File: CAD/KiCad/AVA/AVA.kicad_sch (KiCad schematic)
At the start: 44 parts, among them J1 Conn_01x03_Pin, J10 Conn_01x04_Pin, J2 Conn_01x03_Pin, J3 Conn_01x03_Pin, J4 Conn_01x03_Pin, J5 Conn_01x02_Pin, J6 Conn_01x02_Pin, J7 Conn_01x02_Pin, J8 Conn_01x03_Pin, J9 Conn_01x03_Pin, U1 WEMOS_C3_mini

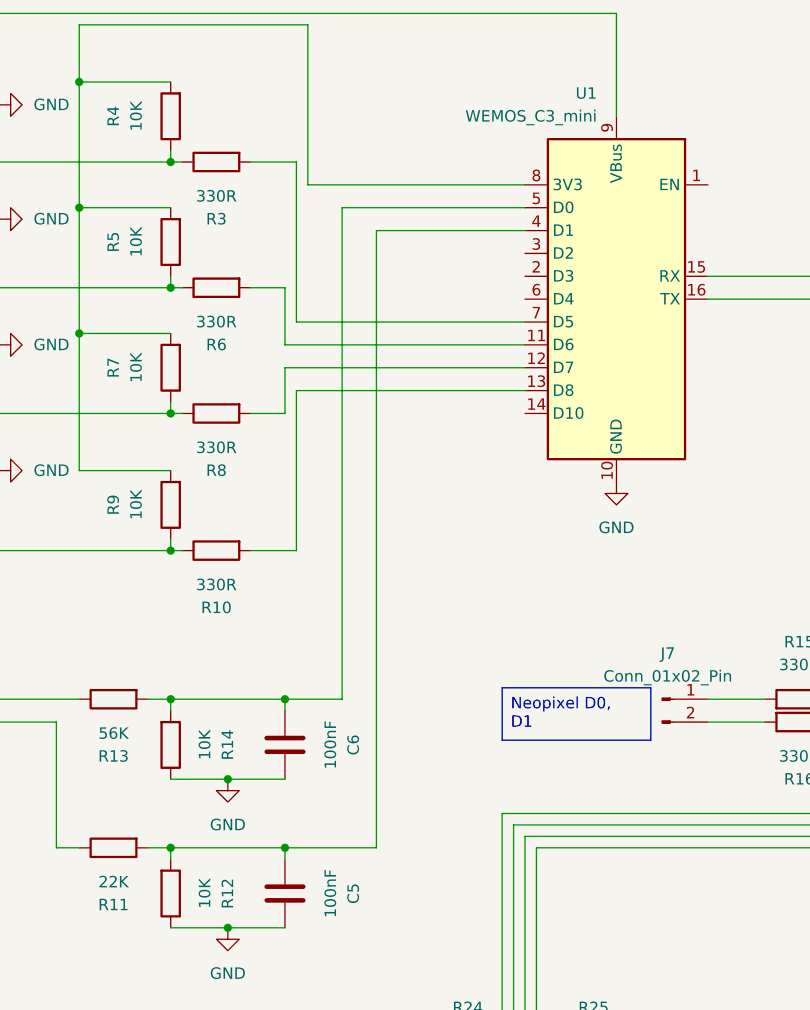
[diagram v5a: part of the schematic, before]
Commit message: Added PCB constraints from other projects which used photomedia etching of layout. Works good enough, 0.35mm track width min and 0.65mm clearance most important. Or else high chance of copper bridges
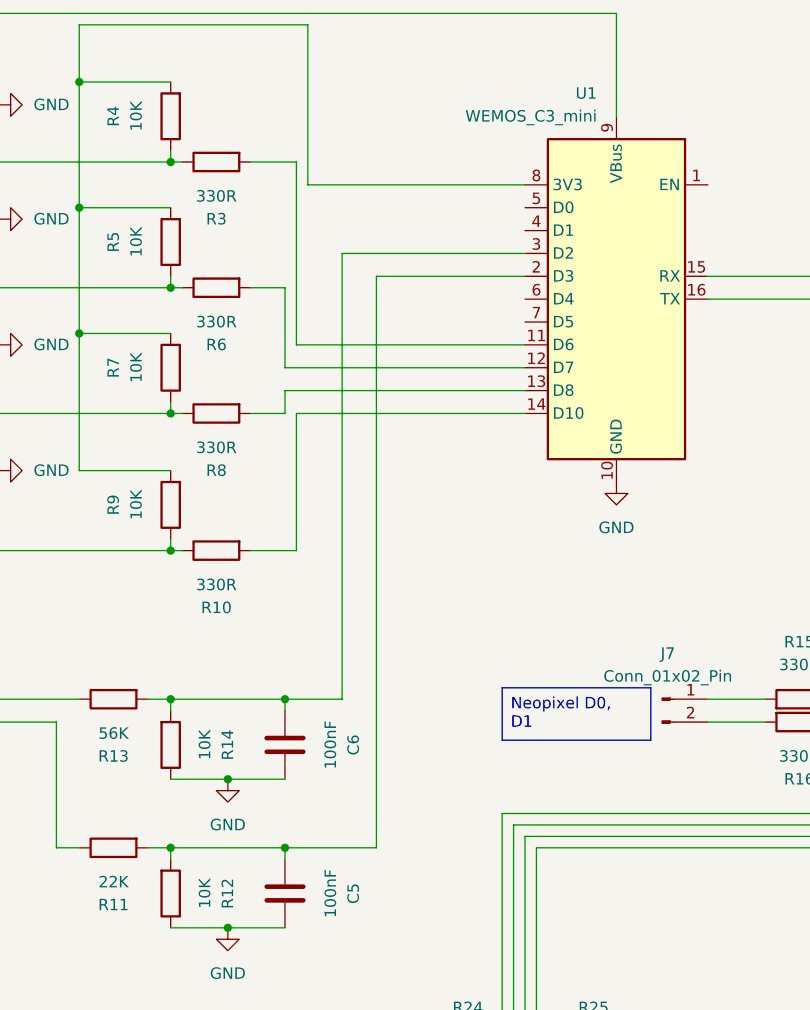
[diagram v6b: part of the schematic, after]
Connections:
- net at C6.2, R13.2, R14.2: now also U1.3 (D2); no longer U1.5 (D0)
- net at C5.2, R11.2, R12.2: now also U1.2 (D3); no longer U1.4 (D1)
- net at R8.2: now also U1.13 (D8); no longer U1.12 (D7)
- net at R10.2: now also U1.14 (D10); no longer U1.13 (D8)
- net at R3.2: now also U1.11 (D6); no longer U1.7 (D5)
- net at R6.2: now also U1.12 (D7); no longer U1.11 (D6)
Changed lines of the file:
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@@
+	(wire
+		(pts
+			(xy 107.95 55.88) (xy 124.46 55.88)
+		)
+		(stroke
+			(width 0)
+			(type default)
+		)
+	)
 	(wire
 		(pts
@@
 	(wire
 		(pts
-			(xy 97.79 57.15) (xy 97.79 63.5)
+			(xy 97.79 57.15) (xy 97.79 66.04)
 		)
 		(stroke
@@
 	(wire
 		(pts
-			(xy 99.06 43.18) (xy 99.06 60.96)
-		)
-		(stroke
-			(width 0)
-			(type default)
-		)
-	)
-	(wire
-		(pts
 			(xy 49.53 182.88) (xy 76.2 182.88)
 		)
@@
 	(wire
 		(pts
-			(xy 97.79 71.12) (xy 97.79 66.04)
-		)
-		(stroke
-			(width 0)
-			(type default)
-		)
-	)
-	(wire
-		(pts
-			(xy 107.95 50.8) (xy 124.46 50.8)
+			(xy 97.79 71.12) (xy 97.79 68.58)
 		)
 		(stroke
@@
 	(wire
 		(pts
+			(xy 99.06 43.18) (xy 99.06 63.5)
+		)
+		(stroke
+			(width 0)
+			(type default)
+		)
+	)
+	(wire
+		(pts
 			(xy 49.53 140.97) (xy 80.01 140.97)
 		)
@@
 	(wire
 		(pts
-			(xy 97.79 63.5) (xy 124.46 63.5)
+			(xy 99.06 71.12) (xy 124.46 71.12)
 		)
 		(stroke
@@
 	(wire
 		(pts
-			(xy 124.46 60.96) (xy 99.06 60.96)
-		)
-		(stroke
-			(width 0)
-			(type default)
-		)
-	)
-	(wire
-		(pts
 			(xy 186.69 105.41) (xy 185.42 105.41)
 		)
@@
 	(wire
 		(pts
+			(xy 124.46 63.5) (xy 99.06 63.5)
+		)
+		(stroke
+			(width 0)
+			(type default)
+		)
+	)
+	(wire
+		(pts
 			(xy 134.62 26.67) (xy 54.61 26.67)
 		)
@@
 	(wire
 		(pts
-			(xy 99.06 68.58) (xy 124.46 68.58)
-		)
-		(stroke
-			(width 0)
-			(type default)
-		)
-	)
-	(wire
-		(pts
 			(xy 198.12 50.8) (xy 167.64 50.8)
 		)
@@
 	(wire
 		(pts
-			(xy 107.95 119.38) (xy 107.95 50.8)
-		)
-		(stroke
-			(width 0)
-			(type default)
-		)
-	)
-	(wire
-		(pts
-			(xy 99.06 86.36) (xy 99.06 68.58)
+			(xy 107.95 119.38) (xy 107.95 55.88)
+		)
+		(stroke
+			(width 0)
+			(type default)
+		)
+	)
+	(wire
+		(pts
+			(xy 104.14 53.34) (xy 124.46 53.34)
+		)
+		(stroke
+			(width 0)
+			(type default)
+		)
+	)
+	(wire
+		(pts
+			(xy 99.06 86.36) (xy 99.06 71.12)
 		)
 		(stroke
@@
 	(wire
 		(pts
-			(xy 97.79 66.04) (xy 124.46 66.04)
-		)
-		(stroke
-			(width 0)
-			(type default)
-		)
-	)
-	(wire
-		(pts
 			(xy 124.46 118.11) (xy 124.46 177.8)
 		)
@@
 	(wire
 		(pts
-			(xy 104.14 102.87) (xy 104.14 48.26)
+			(xy 104.14 102.87) (xy 104.14 53.34)
 		)
 		(stroke
@@
 	(wire
 		(pts
-			(xy 104.14 48.26) (xy 124.46 48.26)
-		)
-		(stroke
-			(width 0)
-			(type default)
-		)
-	)
-	(wire
-		(pts
 			(xy 147.32 177.8) (xy 146.05 177.8)
 		)
@@
 		)
 		(stroke
+			(width 0)
+			(type default)
+		)
+	)
+	(wire
+		(pts
+			(xy 124.46 66.04) (xy 97.79 66.04)
+		)
+		(stroke
+			(width 0)
+			(type default)
+		)
+	)
+	(wire
+		(pts
+			(xy 97.79 68.58) (xy 124.46 68.58)
+		)
+		(stroke

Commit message: Accidentally used 1W instead of 1/4W resistor footprints. Corrected it
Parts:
- R1, R10, R11, R12, R13, R14, R15, R16, R17, R18, R19, R2, R20, R21, R22, R23, R24, R25, R26, R3, R4, R5, R6, R7, R8, R9: footprint Resistor_THT:R_Axial_DIN0614_L14.3mm_D5.7mm_P20.32mm_Horizontal -> Resistor_THT:R_Axial_DIN0207_L6.3mm_D2.5mm_P10.16mm_Horizontal
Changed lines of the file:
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@@
 			)
 		)
-		(property "Footprint" "Resistor_THT:R_Axial_DIN0614_L14.3mm_D5.7mm_P20.32mm_Horizontal"
+		(property "Footprint" "Resistor_THT:R_Axial_DIN0207_L6.3mm_D2.5mm_P10.16mm_Horizontal"
 			(at 181.61 103.632 90)
 			(hide yes)
@@
 			)
 		)
-		(property "Footprint" "Resistor_THT:R_Axial_DIN0614_L14.3mm_D5.7mm_P20.32mm_Horizontal"
+		(property "Footprint" "Resistor_THT:R_Axial_DIN0207_L6.3mm_D2.5mm_P10.16mm_Horizontal"
 			(at 118.11 145.288 90)
 			(hide yes)
@@
 			)
 		)
-		(property "Footprint" "Resistor_THT:R_Axial_DIN0614_L14.3mm_D5.7mm_P20.32mm_Horizontal"
+		(property "Footprint" "Resistor_THT:R_Axial_DIN0207_L6.3mm_D2.5mm_P10.16mm_Horizontal"
 			(at 83.312 107.95 90)
 			(hide yes)
@@
 			)
 		)
-		(property "Footprint" "Resistor_THT:R_Axial_DIN0614_L14.3mm_D5.7mm_P20.32mm_Horizontal"
+		(property "Footprint" "Resistor_THT:R_Axial_DIN0207_L6.3mm_D2.5mm_P10.16mm_Horizontal"
 			(at 142.24 178.562 90)
 			(hide yes)
@@
 			)
 		)
-		(property "Footprint" "Resistor_THT:R_Axial_DIN0614_L14.3mm_D5.7mm_P20.32mm_Horizontal"
+		(property "Footprint" "Resistor_THT:R_Axial_DIN0207_L6.3mm_D2.5mm_P10.16mm_Horizontal"
 			(at 181.61 104.648 90)
 			(hide yes)
@@
 			)
 		)
-		(property "Footprint" "Resistor_THT:R_Axial_DIN0614_L14.3mm_D5.7mm_P20.32mm_Horizontal"
+		(property "Footprint" "Resistor_THT:R_Axial_DIN0207_L6.3mm_D2.5mm_P10.16mm_Horizontal"
 			(at 118.11 178.562 90)
 			(hide yes)
@@
 			)
 		)
-		(property "Footprint" "Resistor_THT:R_Axial_DIN0614_L14.3mm_D5.7mm_P20.32mm_Horizontal"
+		(property "Footprint" "Resistor_THT:R_Axial_DIN0207_L6.3mm_D2.5mm_P10.16mm_Horizontal"
 			(at 191.77 47.498 90)
 			(hide yes)
@@
 			)
 		)
-		(property "Footprint" "Resistor_THT:R_Axial_DIN0614_L14.3mm_D5.7mm_P20.32mm_Horizontal"
+		(property "Footprint" "Resistor_THT:R_Axial_DIN0207_L6.3mm_D2.5mm_P10.16mm_Horizontal"
 			(at 83.312 124.46 90)
 			(hide yes)
@@
 			)
 		)
-		(property "Footprint" "Resistor_THT:R_Axial_DIN0614_L14.3mm_D5.7mm_P20.32mm_Horizontal"
+		(property "Footprint" "Resistor_THT:R_Axial_DIN0207_L6.3mm_D2.5mm_P10.16mm_Horizontal"
 			(at 90.17 69.342 90)
 			(hide yes)
@@
 			)
 		)
-		(property "Footprint" "Resistor_THT:R_Axial_DIN0614_L14.3mm_D5.7mm_P20.32mm_Horizontal"
+		(property "Footprint" "Resistor_THT:R_Axial_DIN0207_L6.3mm_D2.5mm_P10.16mm_Horizontal"
 			(at 90.17 84.582 90)
 			(hide yes)
@@
 			)
 		)
-		(property "Footprint" "Resistor_THT:R_Axial_DIN0614_L14.3mm_D5.7mm_P20.32mm_Horizontal"
+		(property "Footprint" "Resistor_THT:R_Axial_DIN0207_L6.3mm_D2.5mm_P10.16mm_Horizontal"
 			(at 78.74 101.092 90)
 			(hide yes)
@@
 			)
 		)
-		(property "Footprint" "Resistor_THT:R_Axial_DIN0614_L14.3mm_D5.7mm_P20.32mm_Horizontal"
+		(property "Footprint" "Resistor_THT:R_Axial_DIN0207_L6.3mm_D2.5mm_P10.16mm_Horizontal"
 			(at 154.94 104.648 90)
 			(hide yes)
@@
 			)
 		)
-		(property "Footprint" "Resistor_THT:R_Axial_DIN0614_L14.3mm_D5.7mm_P20.32mm_Horizontal"
+		(property "Footprint" "Resistor_THT:R_Axial_DIN0207_L6.3mm_D2.5mm_P10.16mm_Horizontal"
 			(at 118.11 179.578 90)
 			(hide yes)
@@
 			)
 		)
-		(property "Footprint" "Resistor_THT:R_Axial_DIN0614_L14.3mm_D5.7mm_P20.32mm_Horizontal"
+		(property "Footprint" "Resistor_THT:R_Axial_DIN0207_L6.3mm_D2.5mm_P10.16mm_Horizontal"
 			(at 181.61 50.038 90)
 			(hide yes)
@@
 			)
 		)
-		(property "Footprint" "Resistor_THT:R_Axial_DIN0614_L14.3mm_D5.7mm_P20.32mm_Horizontal"
+		(property "Footprint" "Resistor_THT:R_Axial_DIN0207_L6.3mm_D2.5mm_P10.16mm_Horizontal"
 			(at 132.08 167.132 90)
 			(hide yes)
@@
 			)
 		)
-		(property "Footprint" "Resistor_THT:R_Axial_DIN0614_L14.3mm_D5.7mm_P20.32mm_Horizontal"
+		(property "Footprint" "Resistor_THT:R_Axial_DIN0207_L6.3mm_D2.5mm_P10.16mm_Horizontal"
 			(at 132.08 145.288 90)
 			(hide yes)
@@
 			)
 		)
-		(property "Footprint" "Resistor_THT:R_Axial_DIN0614_L14.3mm_D5.7mm_P20.32mm_Horizontal"
+		(property "Footprint" "Resistor_THT:R_Axial_DIN0207_L6.3mm_D2.5mm_P10.16mm_Horizontal"
 			(at 86.868 81.28 90)
 			(hide yes)
@@
 			)
 		)
-		(property "Footprint" "Resistor_THT:R_Axial_DIN0614_L14.3mm_D5.7mm_P20.32mm_Horizontal"
+		(property "Footprint" "Resistor_THT:R_Axial_DIN0207_L6.3mm_D2.5mm_P10.16mm_Horizontal"
 			(at 78.74 117.602 90)
 			(hide yes)
@@
 			)
 		)
-		(property "Footprint" "Resistor_THT:R_Axial_DIN0614_L14.3mm_D5.7mm_P20.32mm_Horizontal"
+		(property "Footprint" "Resistor_THT:R_Axial_DIN0207_L6.3mm_D2.5mm_P10.16mm_Horizontal"
 			(at 90.17 41.402 90)
 			(hide yes)
@@
 			)
 		)
-		(property "Footprint" "Resistor_THT:R_Axial_DIN0614_L14.3mm_D5.7mm_P20.32mm_Horizontal"
+		(property "Footprint" "Resistor_THT:R_Axial_DIN0207_L6.3mm_D2.5mm_P10.16mm_Horizontal"
 			(at 154.94 103.632 90)
 			(hide yes)
@@
 			)
 		)
-		(property "Footprint" "Resistor_THT:R_Axial_DIN0614_L14.3mm_D5.7mm_P20.32mm_Horizontal"
+		(property "Footprint" "Resistor_THT:R_Axial_DIN0207_L6.3mm_D2.5mm_P10.16mm_Horizontal"
 			(at 86.868 66.04 90)
 			(hide yes)
@@
 			)
 		)
-		(property "Footprint" "Resistor_THT:R_Axial_DIN0614_L14.3mm_D5.7mm_P20.32mm_Horizontal"
+		(property "Footprint" "Resistor_THT:R_Axial_DIN0207_L6.3mm_D2.5mm_P10.16mm_Horizontal"
 			(at 86.868 52.07 90)
 			(hide yes)
@@
 			)
 		)
-		(property "Footprint" "Resistor_THT:R_Axial_DIN0614_L14.3mm_D5.7mm_P20.32mm_Horizontal"
+		(property "Footprint" "Resistor_THT:R_Axial_DIN0207_L6.3mm_D2.5mm_P10.16mm_Horizontal"
 			(at 142.24 179.578 90)
 			(hide yes)
@@
 			)
 		)
-		(property "Footprint" "Resistor_THT:R_Axial_DIN0614_L14.3mm_D5.7mm_P20.32mm_Horizontal"
+		(property "Footprint" "Resistor_THT:R_Axial_DIN0207_L6.3mm_D2.5mm_P10.16mm_Horizontal"
 			(at 90.17 55.372 90)
 			(hide yes)
@@
 			)
 		)
-		(property "Footprint" "Resistor_THT:R_Axial_DIN0614_L14.3mm_D5.7mm_P20.32mm_Horizontal"
+		(property "Footprint" "Resistor_THT:R_Axial_DIN0207_L6.3mm_D2.5mm_P10.16mm_Horizontal"
 			(at 118.11 170.688 90)
 			(hide yes)
@@
 			)
 		)
-		(property "Footprint" "Resistor_THT:R_Axial_DIN0614_L14.3mm_D5.7mm_P20.32mm_Horizontal"
+		(property "Footprint" "Resistor_THT:R_Axial_DIN0207_L6.3mm_D2.5mm_P10.16mm_Horizontal"
 			(at 86.868 38.1 90)
 			(hide yes)
